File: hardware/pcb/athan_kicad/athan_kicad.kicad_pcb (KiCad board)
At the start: 2 copper layers, 183.5 x 127.1 mm, 27 parts, among them J1 USB_C_Receptacle_PowerOnly_6P, J2 AudioJack4, SW1 ui_select, SW2 ui_next, SW3 SW_SPST

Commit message: PCB V2 in progress
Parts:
- removed AXU2: Conn_01x03, TerminalBlock:TerminalBlock_MaiXu_MX126-5.0-03P_1x03_P5.00mm
- G***: moved to B.Cu
- moved SW2 83.7 mm to (122.3, 84.8)
- moved SW1 78.4 mm to (122.3, 68.4)
- moved Power1 73.7 mm to (117.3, 110.6)
- moved J2 67.8 mm to (68.3, 114.0), turned to 90 degrees
- moved prg1 61.6 mm to (68.8, 56.7)
- moved G*** 61.5 mm to (102.8, 81.6), turned to 180 degrees
- moved relay1 55.8 mm to (131.5, 111.8), turned to 90 degrees
- moved OLED1 53.5 mm to (94.0, 58.0)
- moved R1 48.9 mm to (60.0, 82.9)
- moved H3 46.4 mm to (62.5, 92.8)
- moved C1 44.5 mm to (69.5, 91.4)
- moved reg1 43.9 mm to (72.0, 102.2)
- moved H4 43.1 mm to (132.9, 98.8)
- moved C3 39.8 mm to (116.9, 100.0)
- moved J_Rx1 39.2 mm to (79.0, 90.2), turned to 90 degrees
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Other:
- board size 183.5 x 127.1 mm -> 77.3 x 60.4 mm
- board text removed: "L"
- board text removed: "R"

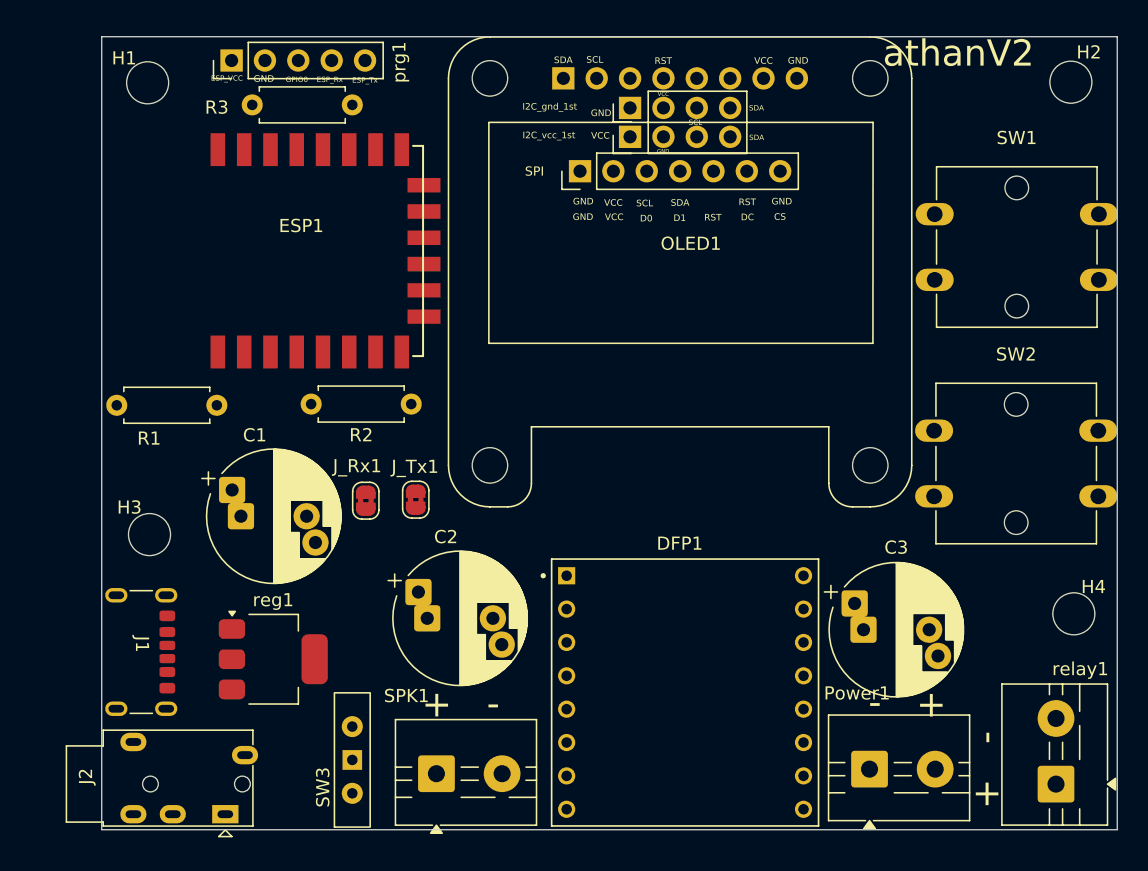
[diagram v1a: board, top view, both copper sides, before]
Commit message: enhancing schematic: adding 1k resistor before dfplayer Rx for eleminating potential buzzing. changing AUX jack footprint from PJ320E to PJ320A which is a mirrored image (more available on stores). PCB not complete yet
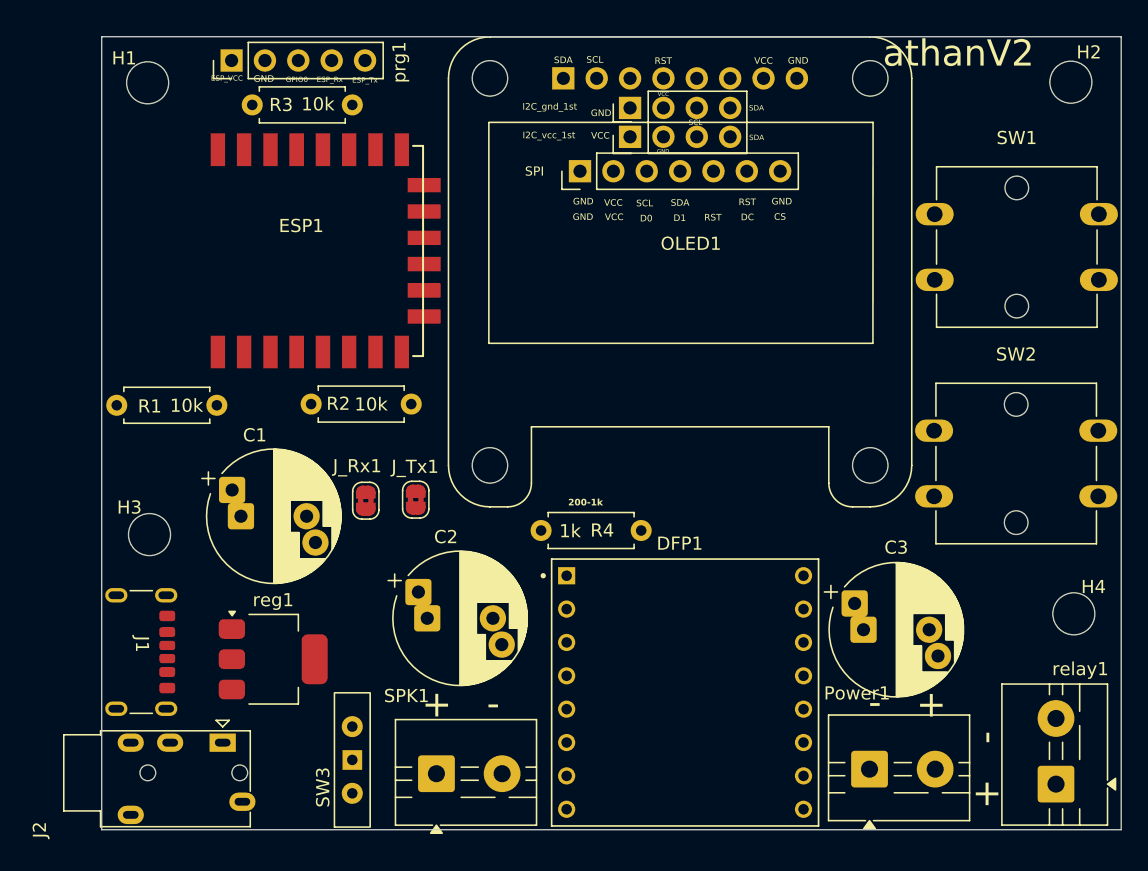
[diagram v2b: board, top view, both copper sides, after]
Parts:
- added R4: 1k, Resistor_THT:R_Axial_DIN0207_L6.3mm_D2.5mm_P7.62mm_Horizontal, F.Cu at (100.0, 92.5)
- J2: footprint Connector_Audio:Jack_3.5mm_PJ320E_Horizontal -> Connector_Audio:Jack_3.5mm_PJ320A_Horizontal
- moved J2 0.87 mm to (68.1, 113.2)
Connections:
- J_Tx1 pad 1: Net-(DFP1-RX) -> Net-(J_Tx1-A)
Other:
- board size 77.3 x 60.4 mm -> 77.6 x 60.4 mm
- board text added: "200-1k"

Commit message: athanV2 PCB finished (hopefully)
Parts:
- moved SW3 12.4 mm to (90.4, 110.0)
- moved prg1 9.22 mm to (78.0, 56.8), turned to -90 degrees
- moved SPK1 6.92 mm to (77.5, 111.0)
- moved R3 4.65 mm to (75.0, 60.2)
- moved H3 2.26 mm to (62.4, 90.5)
- moved G*** 1.54 mm to (102.5, 80.0)
- moved R1 1.37 mm to (61.4, 82.8)
- moved C2 0.93 mm to (84.5, 99.5)
- moved J_Rx1 0.73 mm to (79.7, 90.0)
- moved R4 0.54 mm to (100.5, 92.5)
- moved Power1 0.28 mm to (117.3, 110.9)
- moved H2 0.24 mm to (132.9, 58.4)
- moved H4 0.21 mm to (132.9, 99.0)
- moved J2 0.20 mm to (68.1, 113.0)
- moved OLED1 0.18 mm to (94.0, 58.2)
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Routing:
- net +5V: track 0.00 -> 154.8 mm
- net /ESP_VCC: track 0.00 -> 86.8 mm, vias 0 -> 1
- net /relay: track 0.00 -> 86.6 mm, vias 0 -> 1
- net /GPIO12: track 0.00 -> 78.2 mm, vias 0 -> 1
- net /GPIO14: track 0.00 -> 72.7 mm, vias 0 -> 1
- net GND: track 0.00 -> 59.8 mm, vias 0 -> 128
- net /oled_rst: track 0.00 -> 57.2 mm, vias 0 -> 2
- net /SDA: track 0.00 -> 55.8 mm
- net /SCL: track 0.00 -> 47.4 mm
- net /ESP_Tx: track 0.00 -> 44.1 mm
- net /ESP_Rx: track 0.00 -> 37.0 mm, vias 0 -> 2
- net /AUX_R: track 0.00 -> 32.2 mm
- net /AUX_L: track 0.00 -> 27.4 mm
- net Net-(DFP1-TX): track 0.00 -> 18.9 mm
- net /SPK+: track 0.00 -> 14.4 mm
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- added copper zone on B.Cu, net GND
- added copper zone on F.Cu, net GND
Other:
- board size 77.6 x 60.4 mm -> 78.3 x 60.4 mm
